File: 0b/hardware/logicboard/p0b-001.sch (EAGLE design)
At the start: 24 parts, among them IC1 7404D, IC4 LTC485S, IC5 LTC485S, J0 DC5V, J7 DIN5, J9 DIN5, X7 NELTRON-7810-XPXC

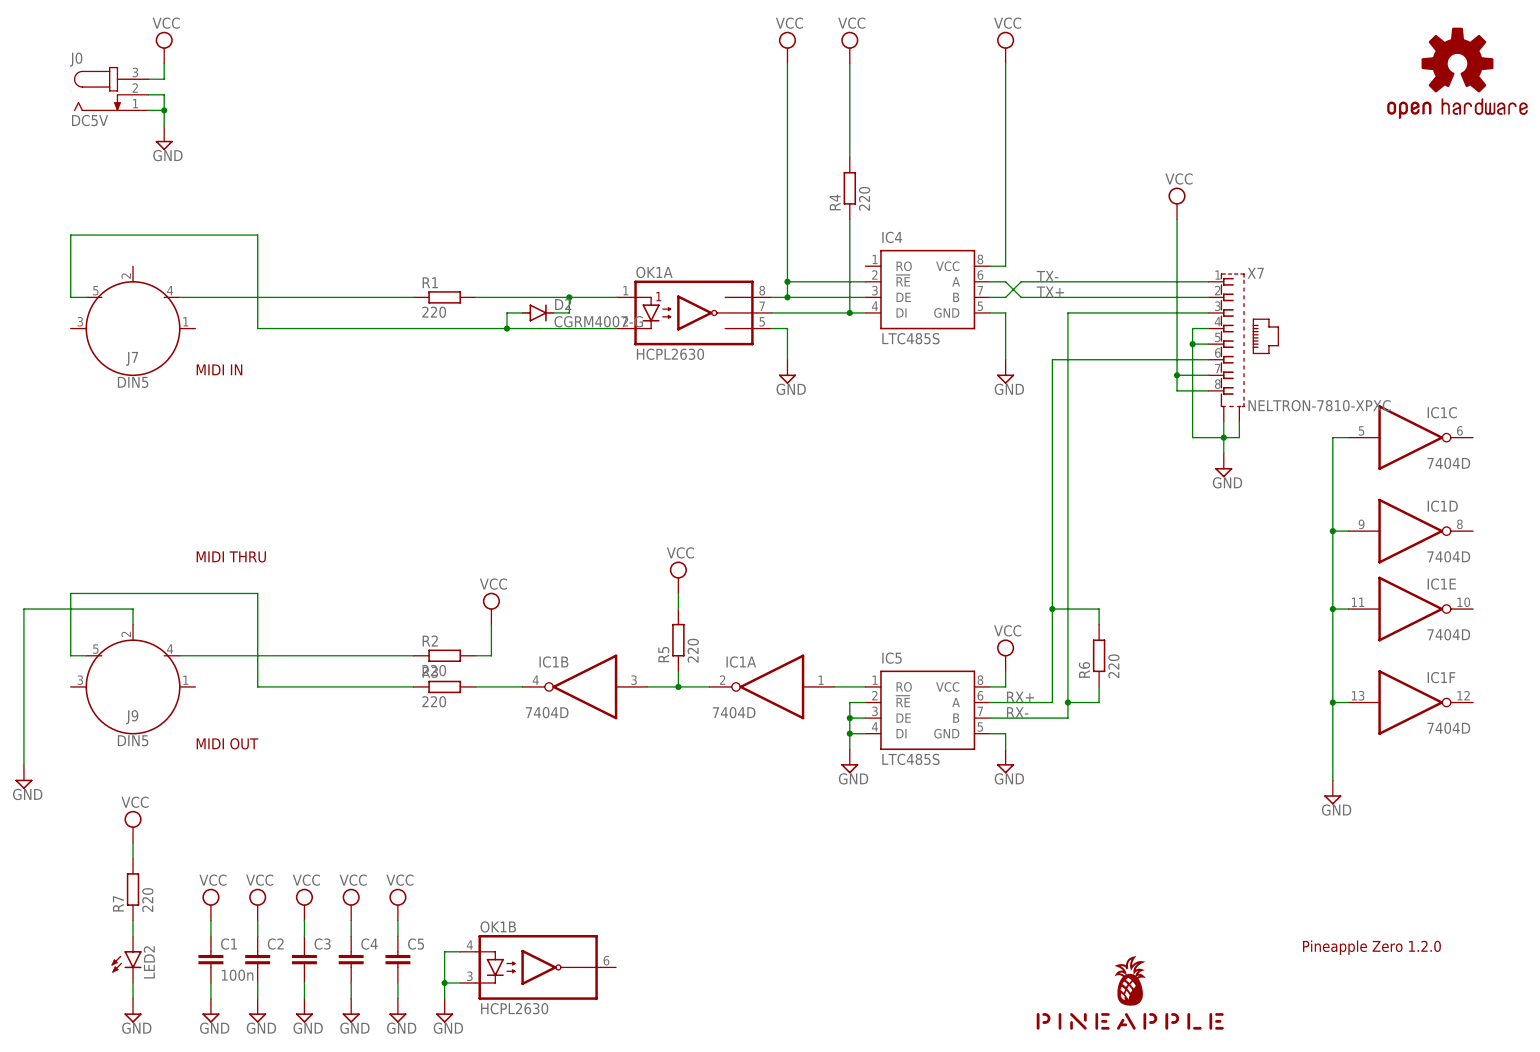
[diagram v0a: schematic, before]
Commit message: Now runs by 7805 regulator.
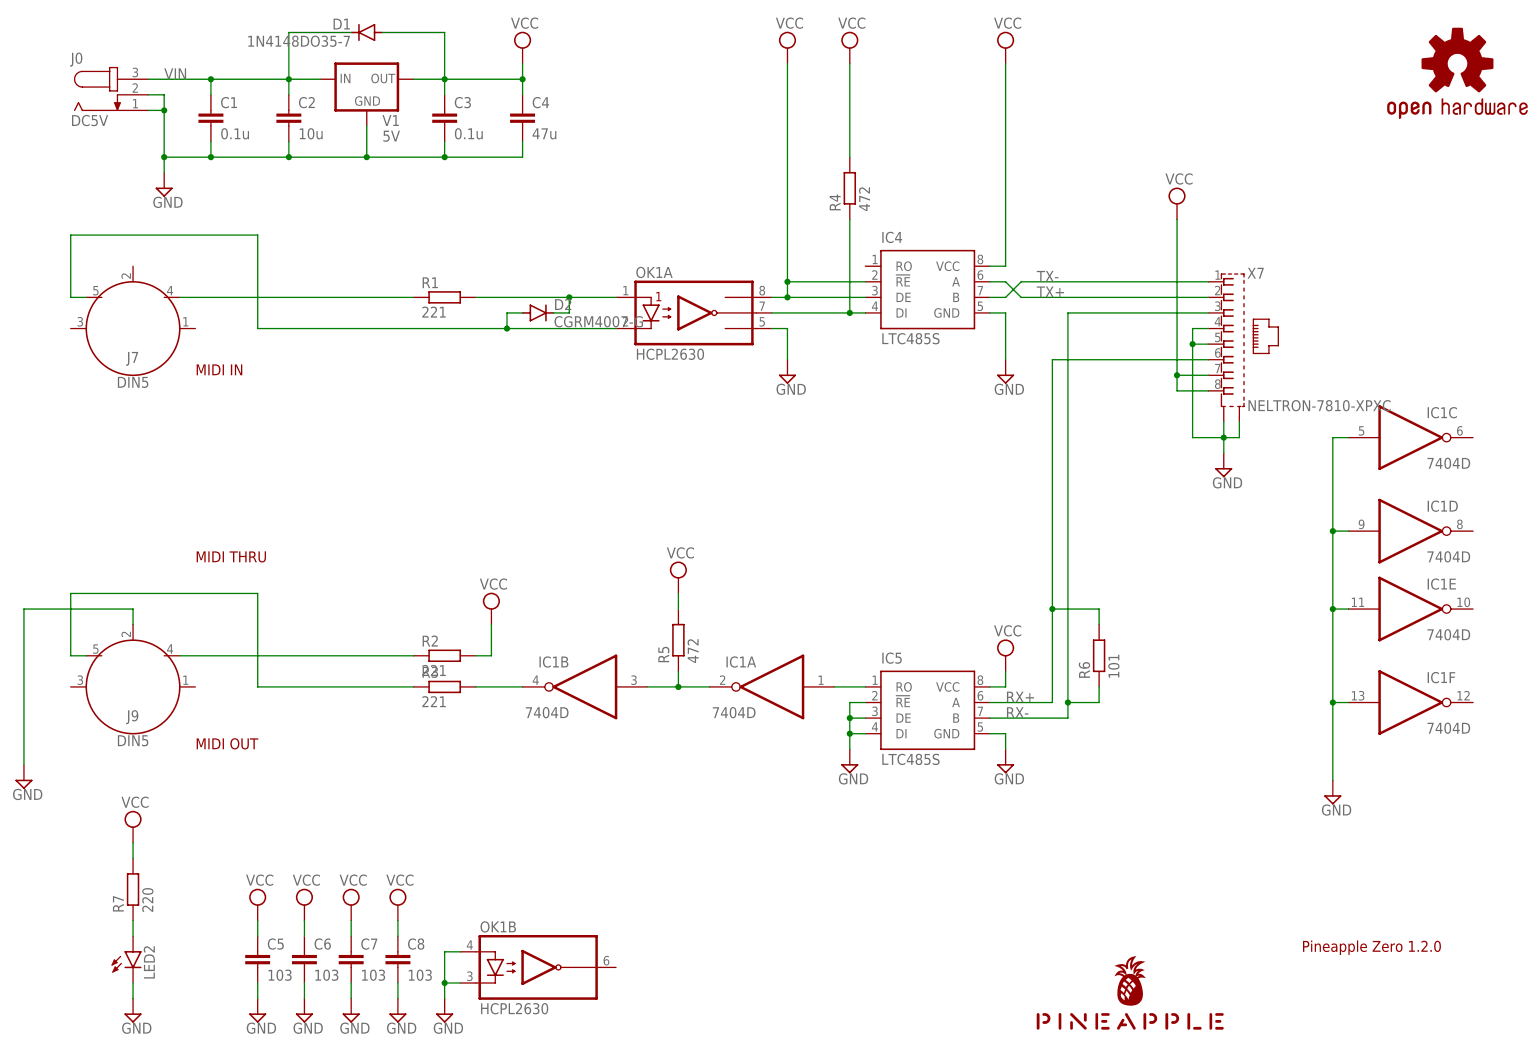
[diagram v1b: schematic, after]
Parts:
- added C6, C7, C8: 103, rcl:C-EUC1206
- added D1: 1N4148DO35-7, diode:1N4148DO35-7
- added V1: 5V, v-reg:78XXS
- C1: value 100n -> 0.1u; device rcl:C-EU025-024X044 -> rcl:C-EU025-025X050
- C2: value (none) -> 10u; device rcl:C-EUC1206 -> rcl:C-EU025-030X050
- C3: value (none) -> 0.1u; device rcl:C-EUC1206 -> rcl:C-EU025-025X050
- C4: value (none) -> 47u; device rcl:C-EUC1206 -> rcl:C-EU025-050X050
- C5: value (none) -> 103
- R1, R2, R3: value 220 -> 221
- R4, R5: value 220 -> 472
- R6: value 220 -> 101
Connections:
- new net VIN: C1.1, C2.1, D1.C, J0.3, V1.IN
- net GND: now also C6.2, C7.2, C8.2, V1.GND
- net VCC: now also C6.1, C7.1, C8.1, D1.A, V1.OUT; no longer C1.1, C2.1, J0.3
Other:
- moved on the sheet: C1, C2, C3, C4, C5

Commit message: Fixed pinout of 0b.
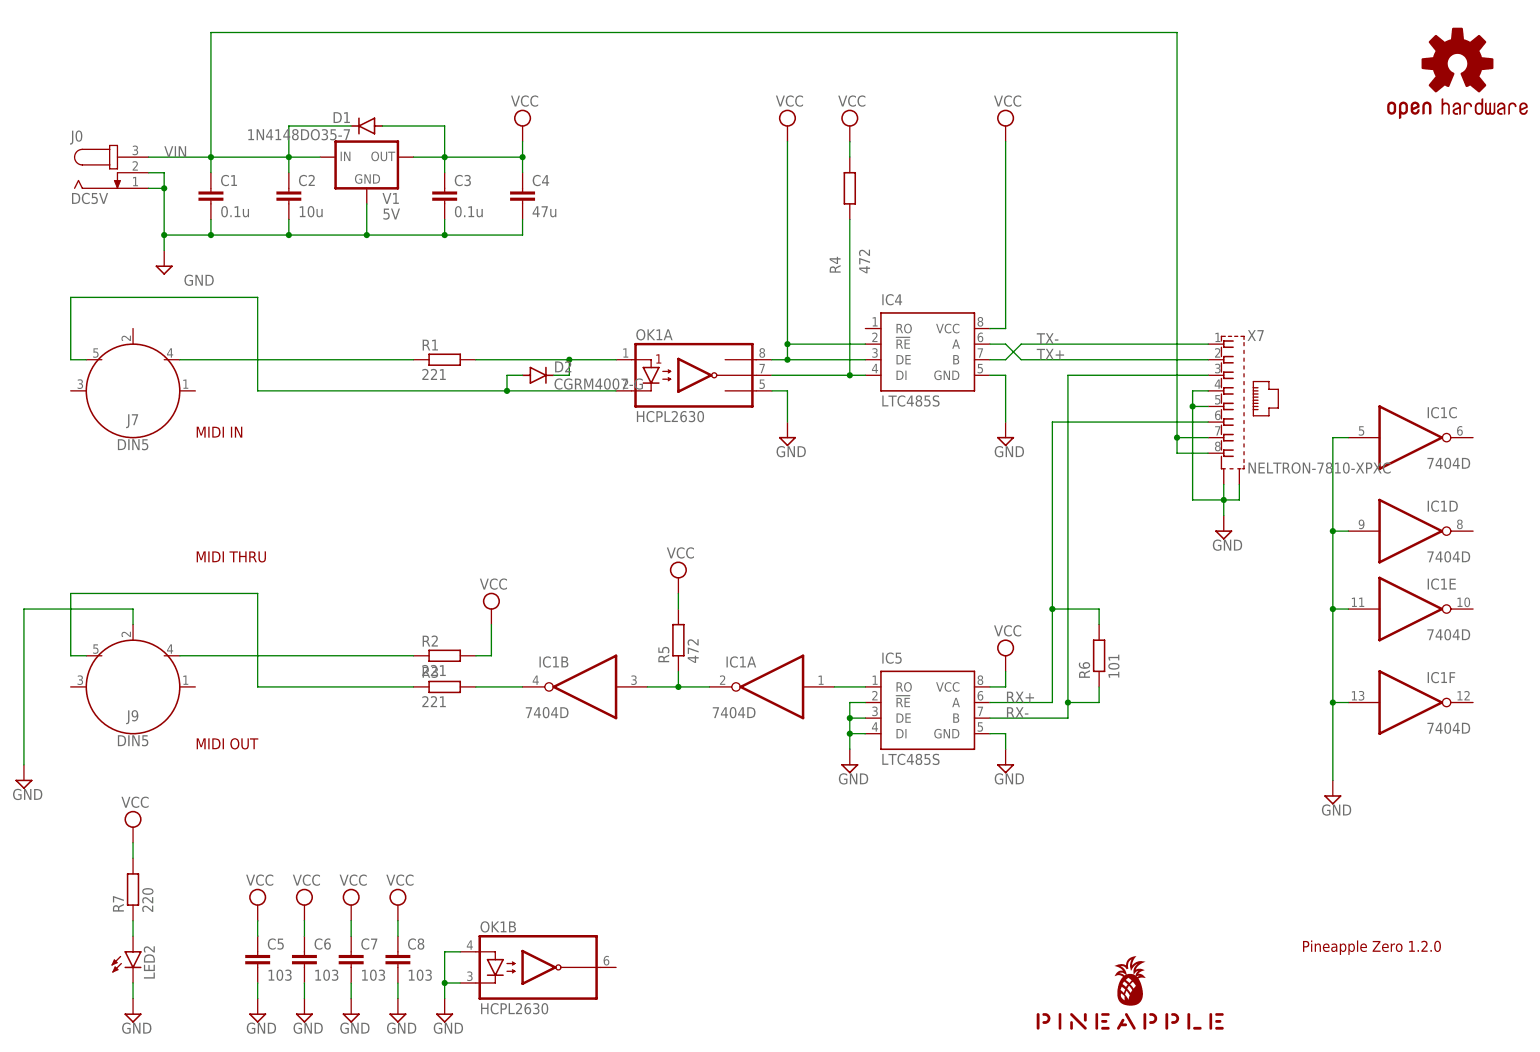
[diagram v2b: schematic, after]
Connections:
- net VCC: no longer X7.7, X7.8
- net VIN: now also X7.7, X7.8
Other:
- moved on the sheet: C1, C2, C3, C4, D1, D2, IC4, J0, J7, OK1A, R1, V1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

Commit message: MIDI Phantom.
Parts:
- added S1: MIDIPHANTOM, switch-dil:DIP04YL
- OK1: value HCPL2630 -> HCPL0600; device optocoupler:HCPL2630 -> optocoupler:HCPL0600
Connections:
- removed net VIN: C1.1, C2.1, D1.C, J0.3, V1.IN, X7.7, X7.8
- new net MIDIINGND: J7.1, S1.1
- new net MIDIINV+: J7.3, S1.2
- new net MIDIOUTGND: J9.1, S1.3
- new net MIDIOUTV+: J9.3, S1.4
- new net V+: C1.1, C2.1, D1.C, J0.3, S1.5, S1.7, V1.IN, X7.7, X7.8
- net GND: now also OK1.GND, S1.6, S1.8; no longer OK1A.GND, OK1B.A2, OK1B.C2
- net MIDIIN: now also OK1.A; no longer OK1A.A1
- net MIRTN: now also OK1.C; no longer OK1A.C1
- net TX: now also OK1.VO; no longer OK1A.VO1
- net VCC: now also OK1.VCC, OK1.VE; no longer OK1A.VCC
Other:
- note removed: "MIDI THRU"
- moved on the sheet: D2, J7, R1
